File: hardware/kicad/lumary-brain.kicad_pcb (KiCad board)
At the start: 4 copper layers, 63.3 x 31.3 mm, 32 parts, among them J1 PWR_IN, J2 CN1, J3 USB-C, Q1 NMOS_60V, Q2 NMOS_60V, Q3 AO3401A, SW1 BOOT, SW2 EN, U1 ESP32-H2-MINI-1-N4, U2 ME6211C33M5G, U3 74AHCT1G125, U4 USBLC6-2SC6

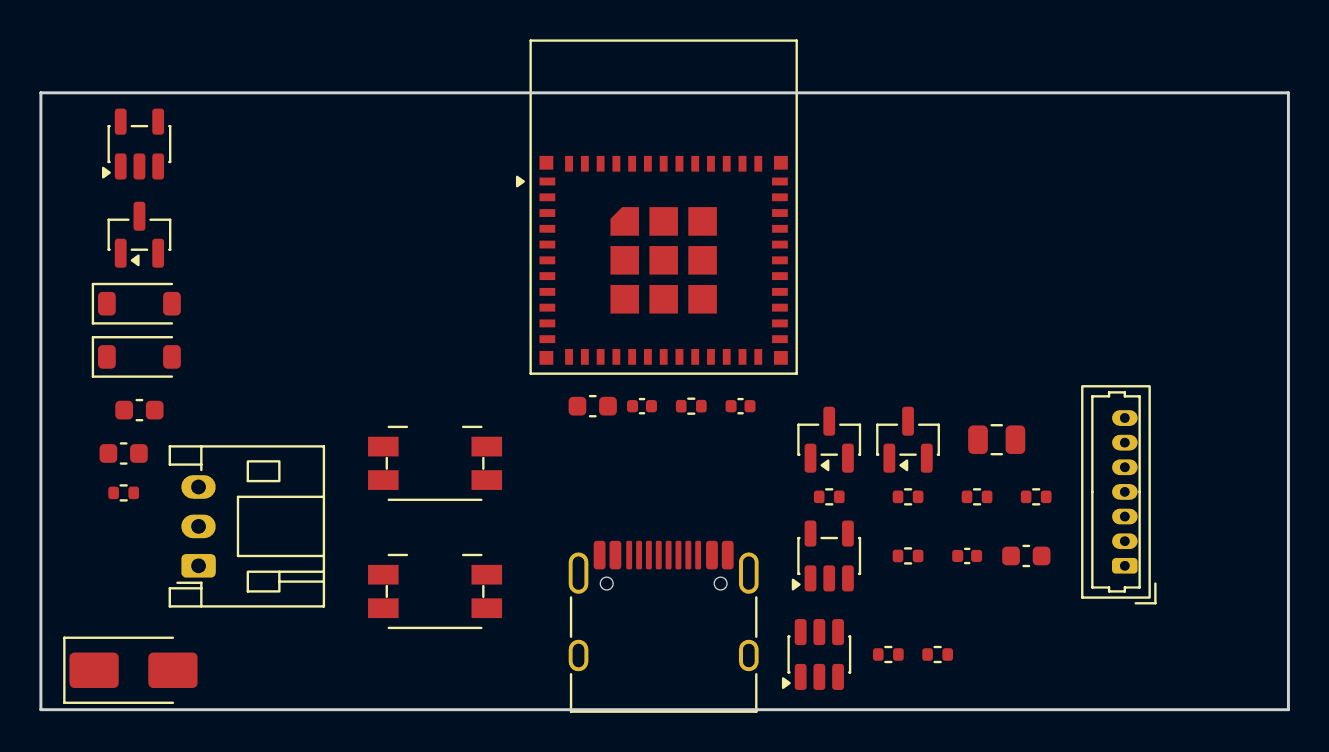
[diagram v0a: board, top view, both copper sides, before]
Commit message: feat(hw): adopt user layout + fix support-part locality
User's placement (module top-left/antenna off left edge, J1 lower-left,
J2 right, USB bottom) adopted as script baseline. Relocated only the
electrically-bound parts: module decoupling to 3V3 pad, USB ESD + CC
pulldowns to the connector, LDO caps to U2 pins, buffer cap to U3,
4V7 bulk to Q3/J2, EN RC near EN pad. DRC: 0 violations.

Co-Authored-By: Claude Opus 4.8 <noreply@anthropic.com>
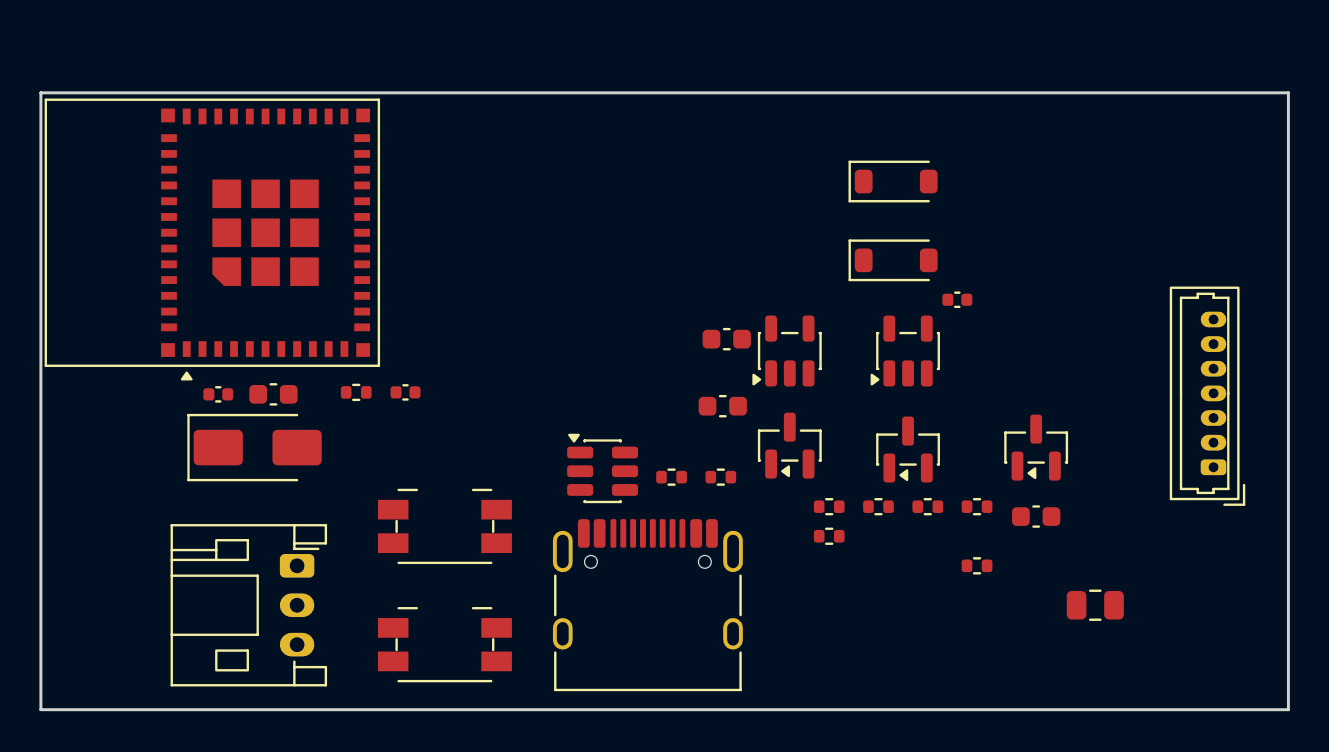
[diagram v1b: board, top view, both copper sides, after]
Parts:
- moved Q3 46.8 mm to (50.5, 18.0)
- moved C4 46.4 mm to (50.5, 21.5)
- moved R9 43.5 mm to (47.5, 24.0)
- moved D1 38.9 mm to (43.4, 4.50)
- moved D2 38.7 mm to (43.4, 8.50)
- moved U2 34.6 mm to (38.0, 13.1)
- moved C3 29.6 mm to (34.6, 15.9)
- moved C6 21.5 mm to (9.00, 15.3)
- moved U1 20.2 mm to (11.4, 7.10), turned to 90 degrees
- moved C2 18.8 mm to (34.8, 12.5)
- moved C8 17.0 mm to (18.5, 15.2)
- moved R6 17.0 mm to (16.0, 15.2)
- moved C5 16.2 mm to (11.8, 15.3)
- moved U4 14.4 mm to (28.5, 19.2), turned to 0 degrees
- moved R7 14.2 mm to (32.0, 19.5)
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
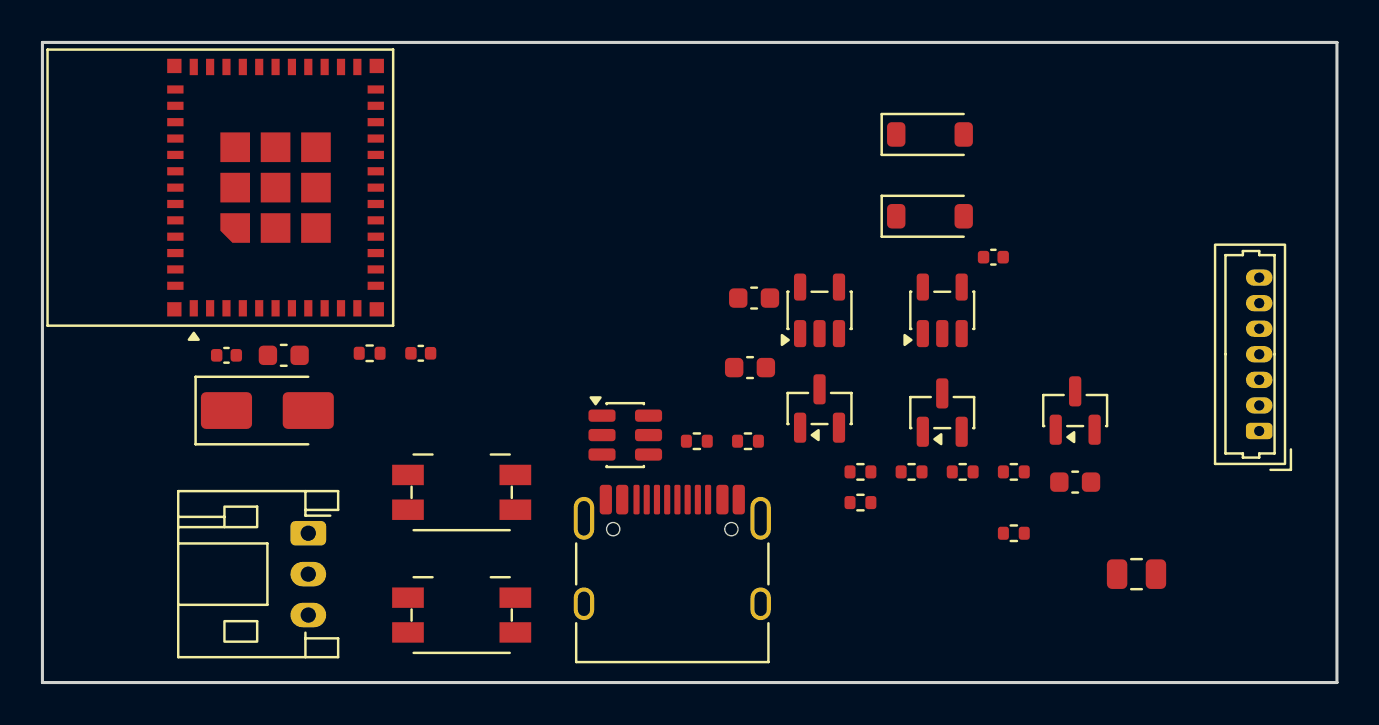
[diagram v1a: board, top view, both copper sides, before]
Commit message: feat(hw): net classes + GND planes on all 4 layers
Project file adds Power (0.5mm) / Default (0.25mm) net classes. Script
now pours GND on F/B + solid planes on In1/In2 (inset 0.6mm, solid pad
connections for reflow, NPTH keepouts at USB pegs). Antenna region
correctly excluded from fill by module rule area. DRC: 0 violations;
airwires 110 -> 49 (signals only).

Co-Authored-By: Claude Opus 4.8 <noreply@anthropic.com>
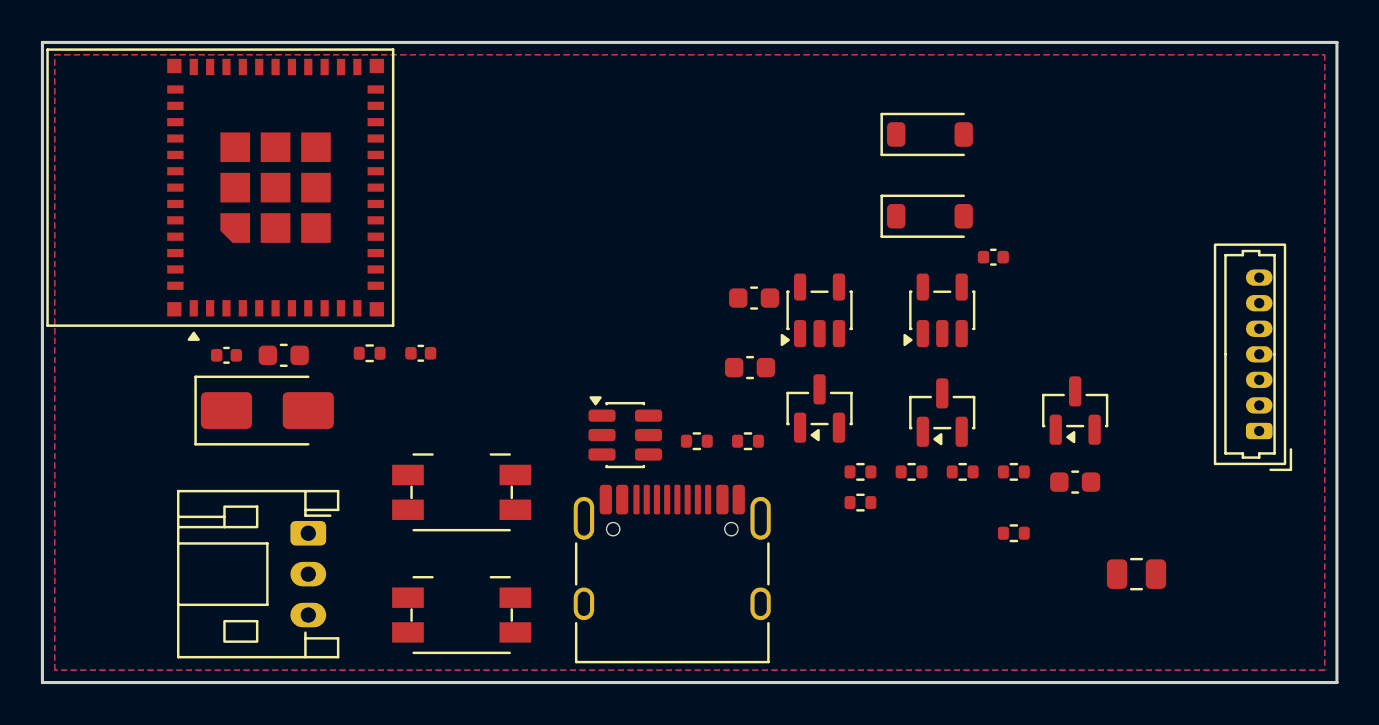
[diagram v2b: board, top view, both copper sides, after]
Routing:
- added copper zone on B.Cu, net GND
- added copper zone on F.Cu, net GND
- added copper zone on In1.Cu, net GND
- added copper zone on In2.Cu, net GND

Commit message: feat(hw): rounded board ends matching case (18mm arcs)
Outline redrawn: straight top/bottom + single 18mm-radius arc each end
(sagitta ~9.1mm -> ~45mm straight section, matches user's ~44mm
measurement). Zone outlines follow the shape with radial 0.6mm inset.
Left cluster (U1/J1/SWs/caps/D3) shifted to clear the deeper corner
cuts and the antenna keepout. DRC: 0 electrical violations (2 waivable
module-silk-at-edge warnings).

Co-Authored-By: Claude Opus 4.8 <noreply@anthropic.com>
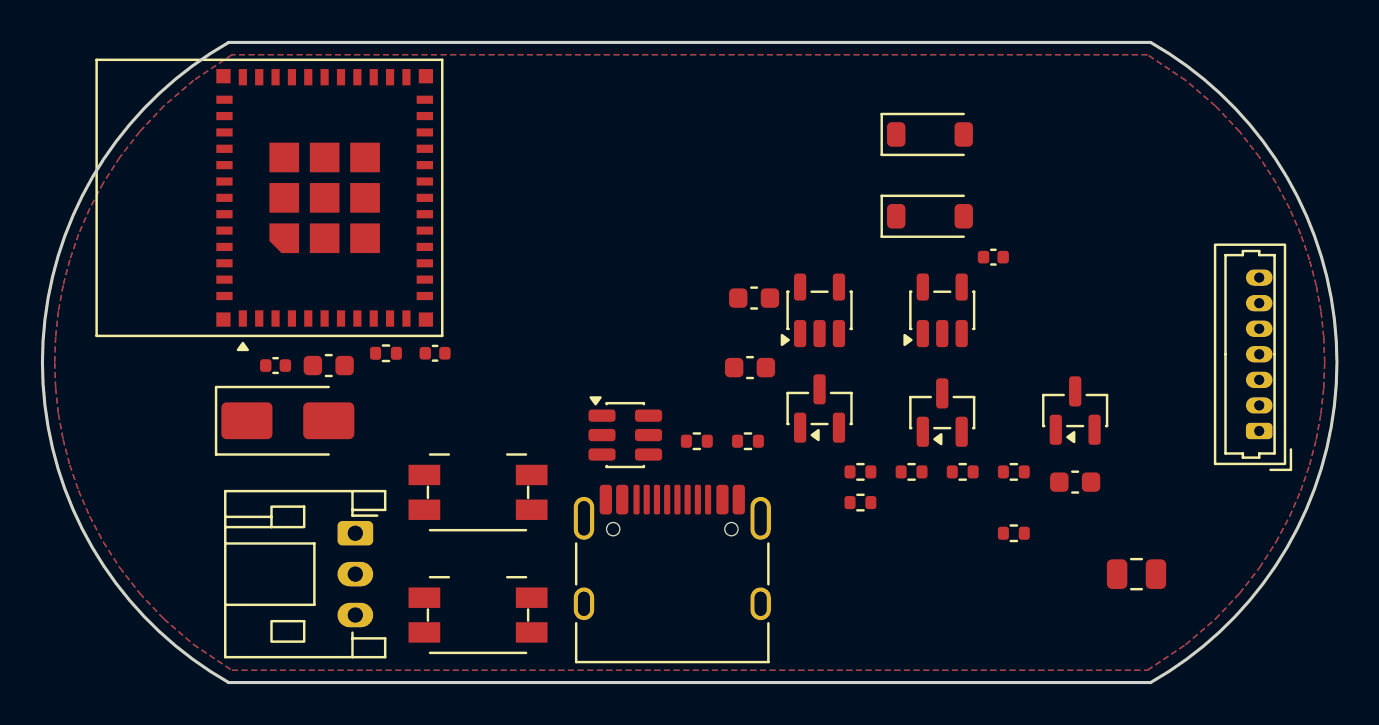
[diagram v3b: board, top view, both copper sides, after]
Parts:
- moved C6 2.45 mm to (11.4, 15.8)
- moved U1 2.45 mm to (13.8, 7.60)
- moved J1 2.30 mm to (15.3, 24.0)
- moved C5 2.26 mm to (14.0, 15.8)
- moved D3 1.12 mm to (12.0, 18.5)
- moved R6 0.80 mm to (16.8, 15.2)
- moved SW1 0.80 mm to (21.3, 22.0)
- moved SW2 0.80 mm to (21.3, 28.0)
- moved C8 0.70 mm to (19.2, 15.2)
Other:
- outline, holes or cut-outs redrawn

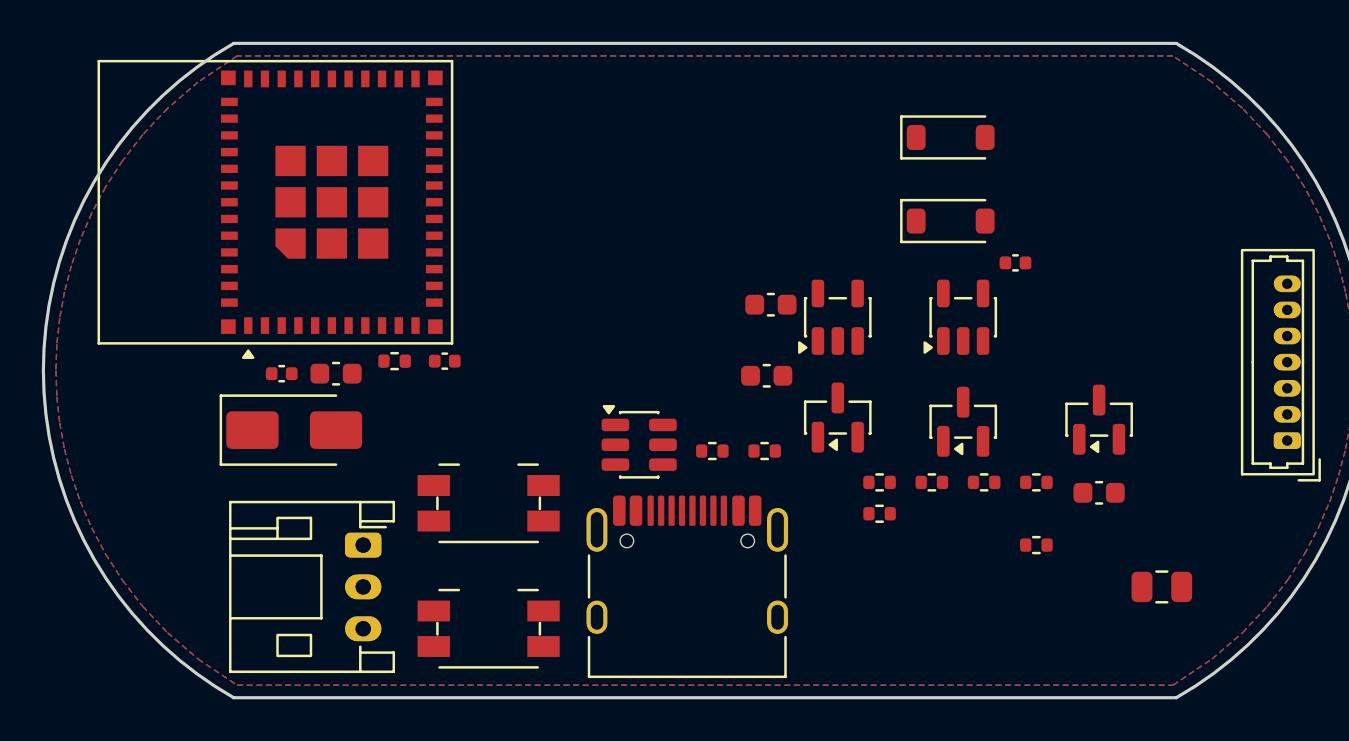
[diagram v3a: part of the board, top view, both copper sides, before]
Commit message: feat(hw): adopt user layout v2
Full user reorganization synced into build script: power cluster
top-center at LDO, USB-C right-of-center with ESD/CC hugging it,
buffer top-right by J2, buttons center, larger antenna dead zone
(x<14.2). DRC 0 violations; all 10 locality checks pass.

Co-Authored-By: Claude Opus 4.8 <noreply@anthropic.com>
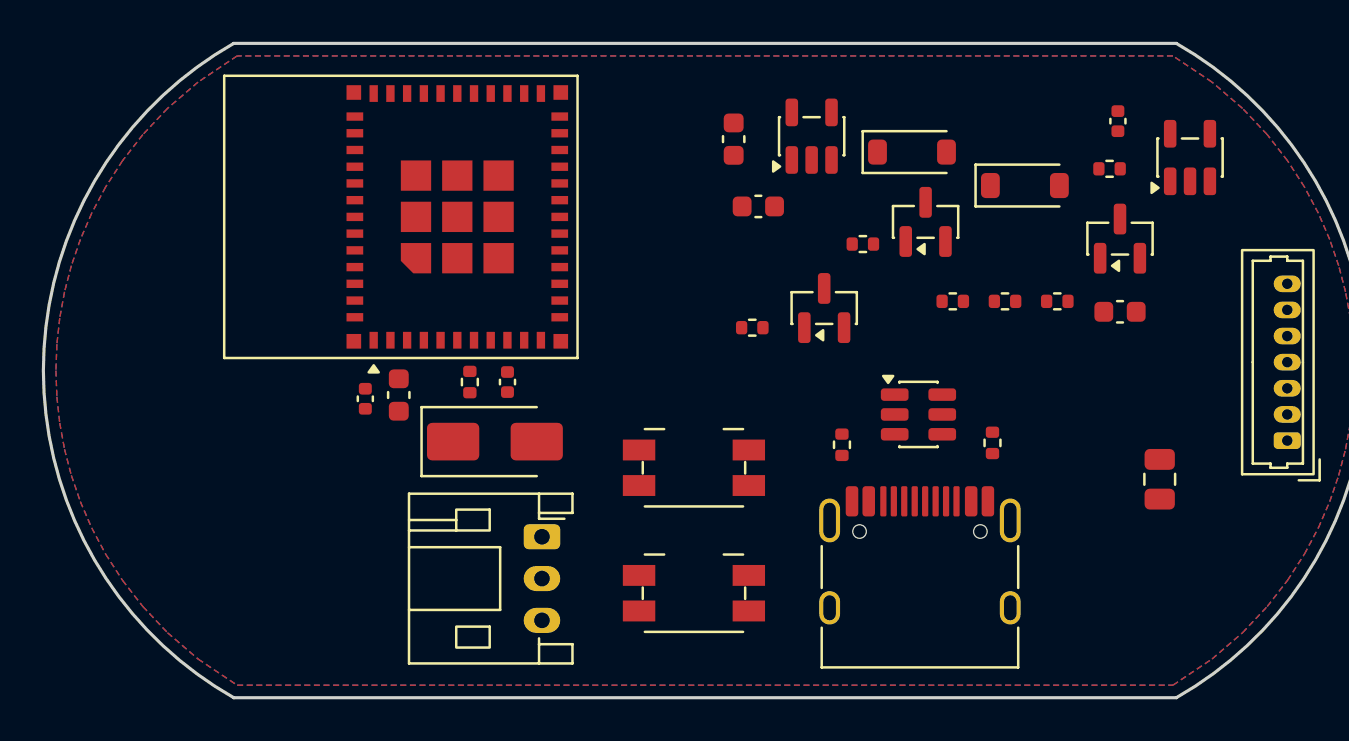
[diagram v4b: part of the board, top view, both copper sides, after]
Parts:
- moved R9 18.3 mm to (51.0, 6.00)
- moved U4 13.4 mm to (41.9, 17.8)
- moved U3 13.3 mm to (54.9, 5.46)
- moved R2 12.9 mm to (39.2, 9.60)
- moved J3 11.1 mm to (41.9, 25.9)
- moved R8 10.9 mm to (45.4, 19.1), turned to 90 degrees
- moved SW1 9.97 mm to (31.1, 20.3)
- moved SW2 9.97 mm to (31.1, 26.3)
- moved Q2 9.73 mm to (42.2, 8.54)
- moved D3 9.62 mm to (21.6, 19.1)
- moved R1 9.58 mm to (33.9, 13.6)
- moved U2 8.75 mm to (36.8, 4.44)
- moved C4 8.72 mm to (51.5, 12.8)
- moved Q3 8.72 mm to (51.5, 9.34)
- moved R3 8.72 mm to (46.0, 12.3)
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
